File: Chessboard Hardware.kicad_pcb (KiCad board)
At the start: 2 copper layers, 199 x 199 mm, 86 parts, among them J1 Conn_01x04_Pin

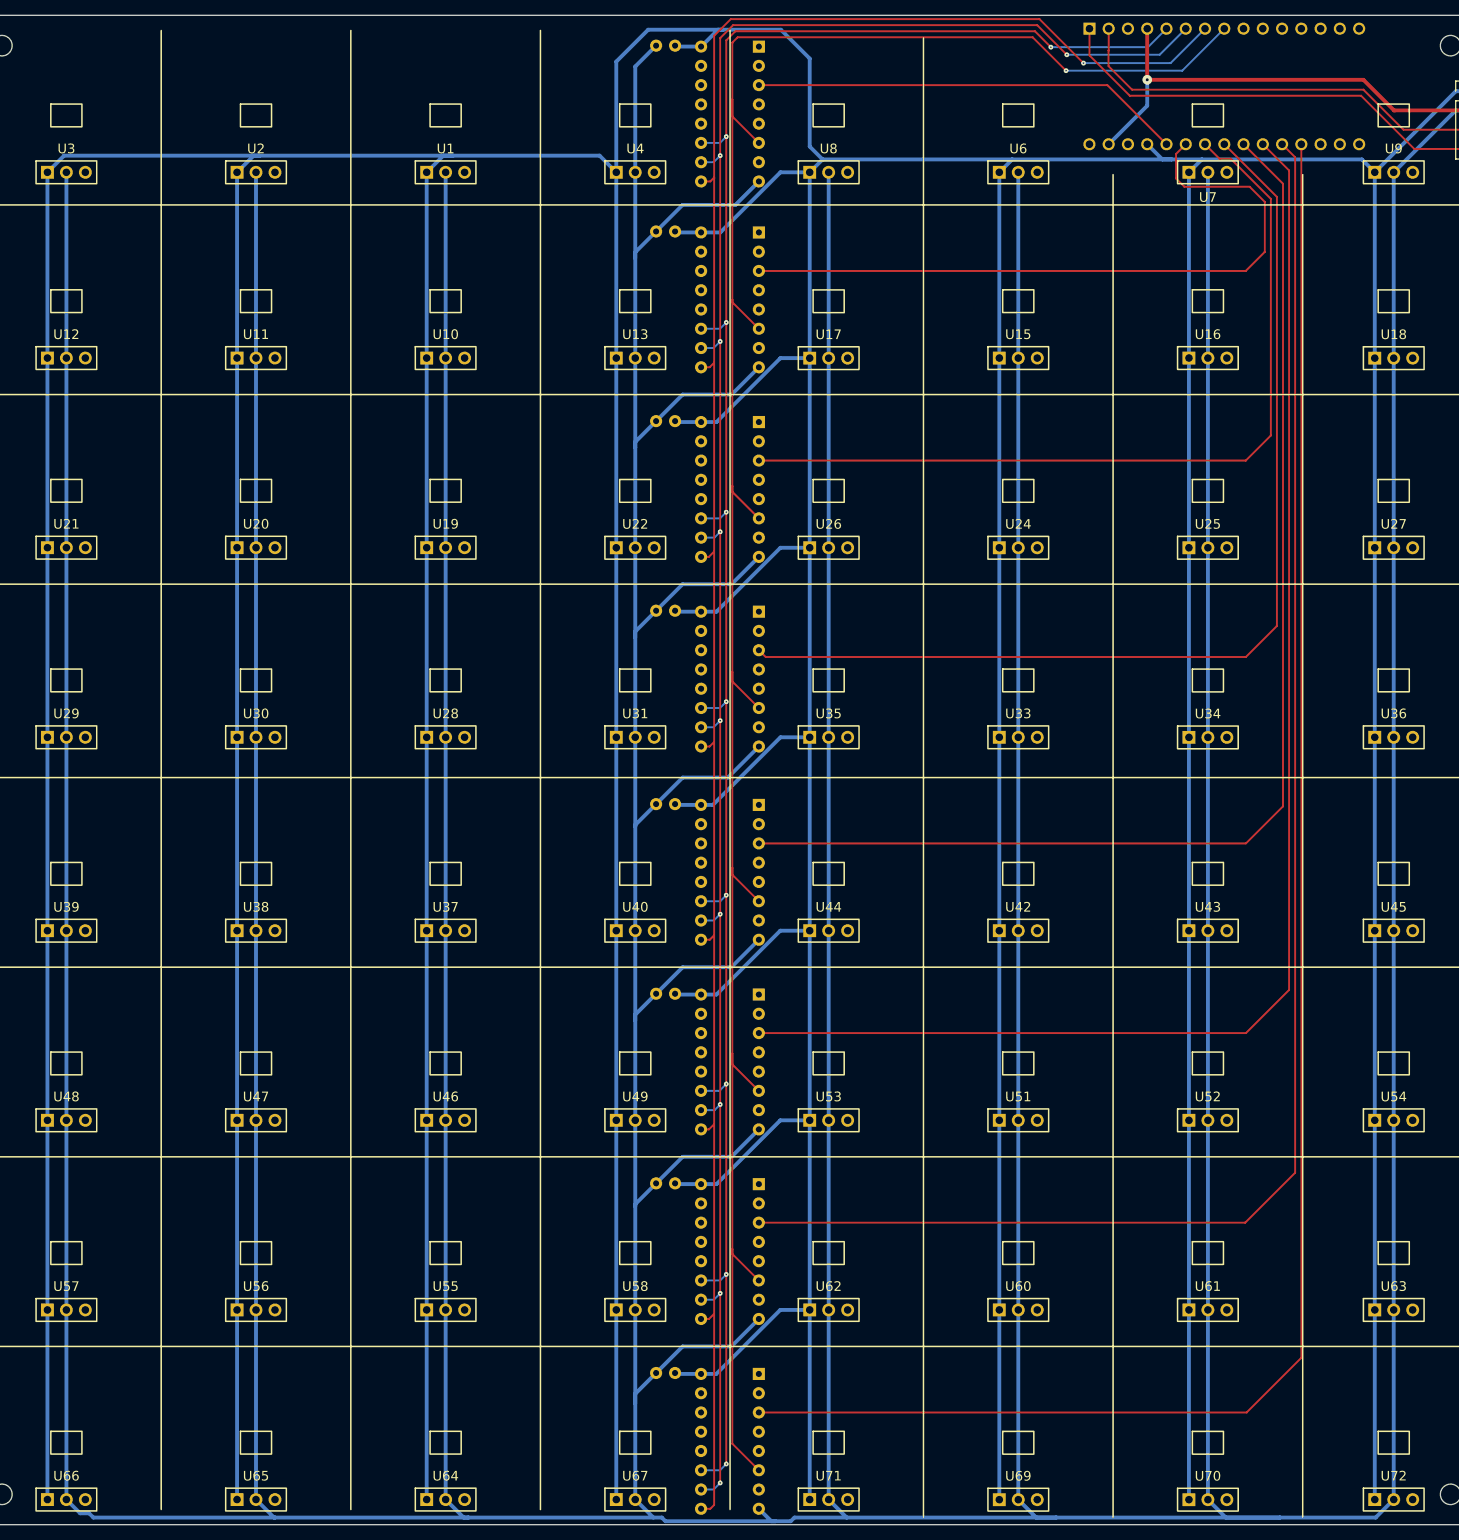
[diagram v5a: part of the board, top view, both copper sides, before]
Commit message: Finish routing
With help from Freerouting
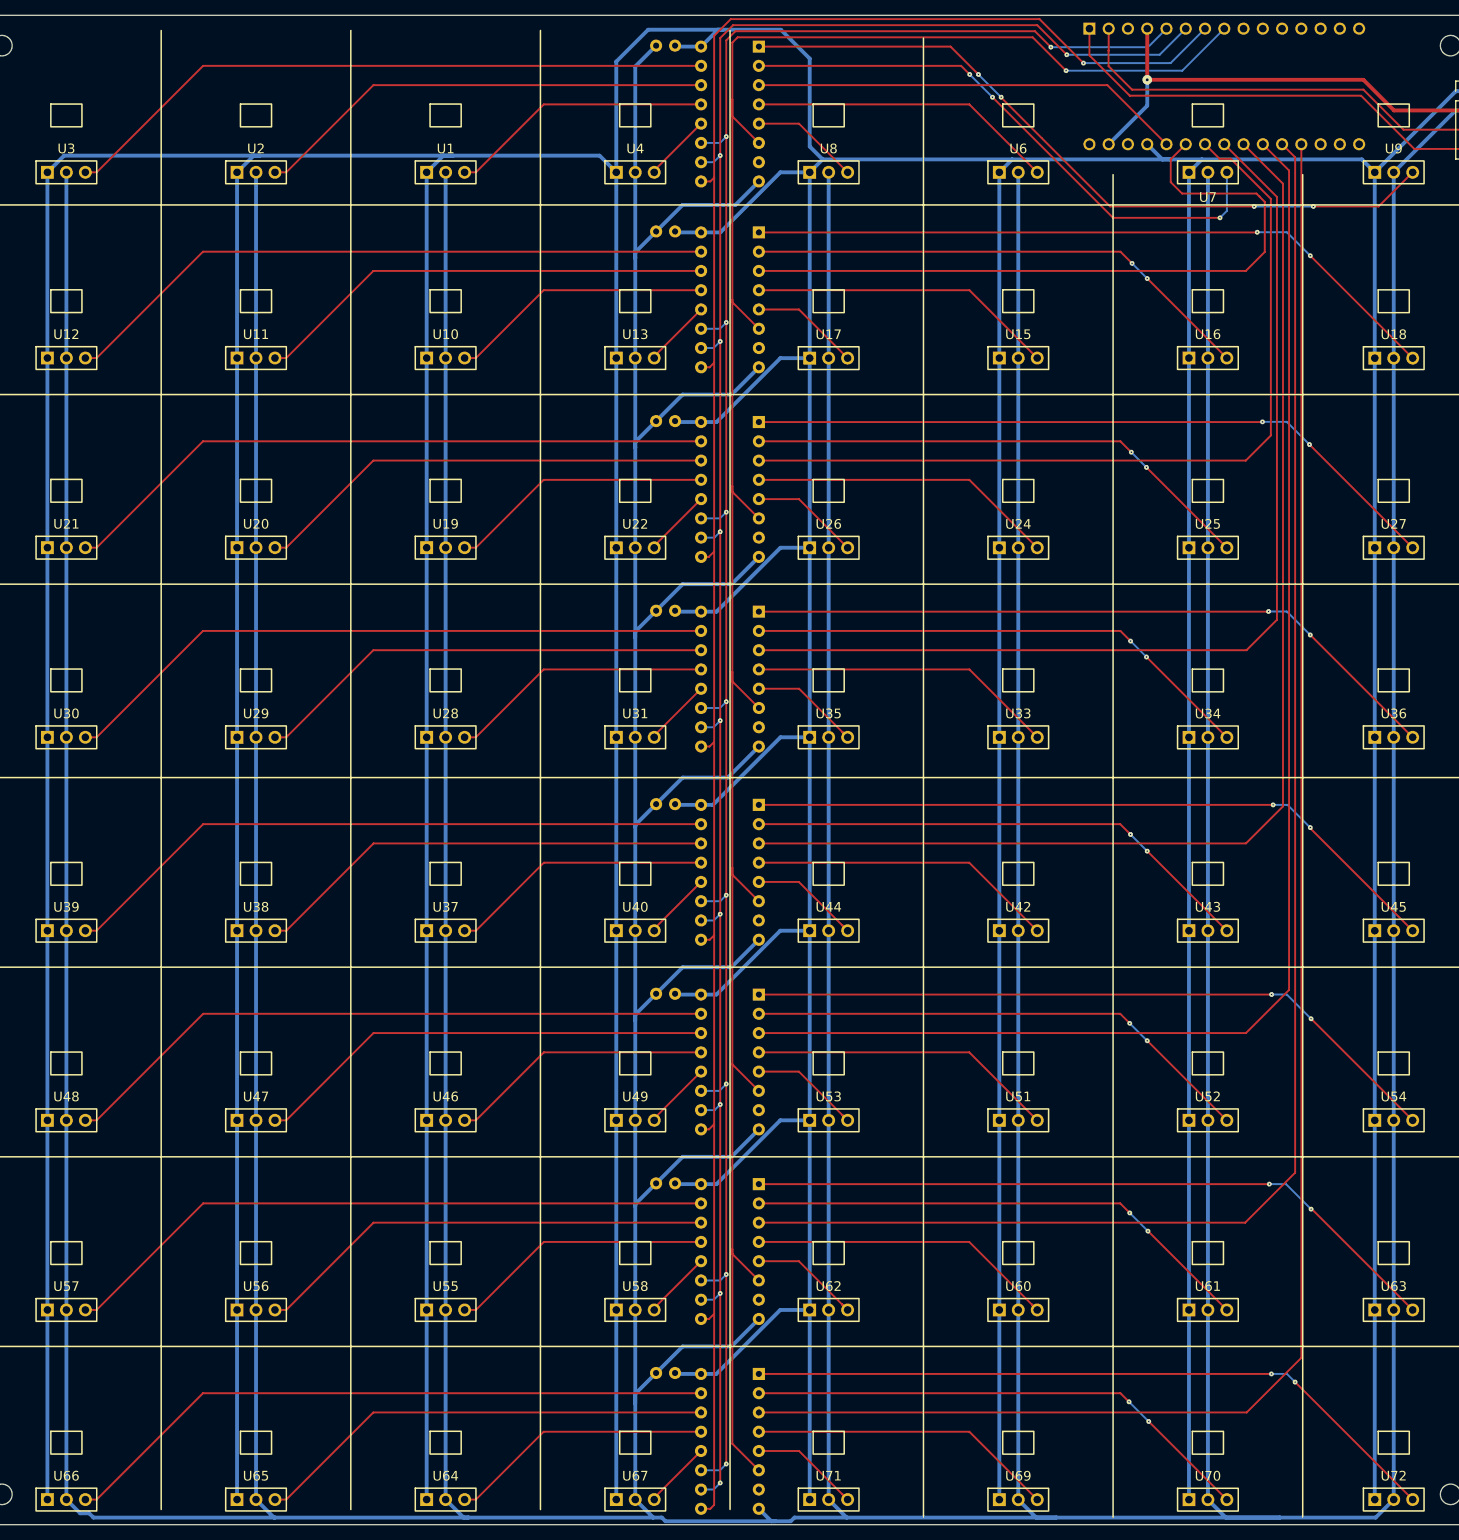
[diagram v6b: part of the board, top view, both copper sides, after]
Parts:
- moved U29 25.0 mm to (87.5, 145.2)
- moved U30 25.0 mm to (62.5, 145.2)
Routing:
- net Net-(U5-Y4): track 0.00 -> 96.8 mm, vias 0 -> 4
- net Net-(U41-Y4): track 0.00 -> 93.1 mm, vias 0 -> 2
- net Net-(U23-Y4): track 0.00 -> 93.1 mm, vias 0 -> 2
- net Net-(U14-Y4): track 0.00 -> 93.1 mm, vias 0 -> 2
- net Net-(U32-Y4): track 0.00 -> 93.1 mm, vias 0 -> 2
- net Net-(U50-Y4): track 0.00 -> 93.1 mm, vias 0 -> 2
- net Net-(U59-Y4): track 0.00 -> 93.1 mm, vias 0 -> 2
- net Net-(U68-Y4): track 0.00 -> 93.1 mm, vias 0 -> 2
- net Net-(U57-SIG): track 0.00 -> 87.0 mm
- net Net-(U39-SIG): track 0.00 -> 87.0 mm
- net Net-(U3-SIG): track 0.00 -> 87.0 mm
- net Net-(U48-SIG): track 0.00 -> 87.0 mm
- net Net-(U21-SIG): track 0.00 -> 87.0 mm
- net Net-(U30-SIG): track 0.00 -> 87.0 mm
- net Net-(U12-SIG): track 0.00 -> 87.0 mm
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
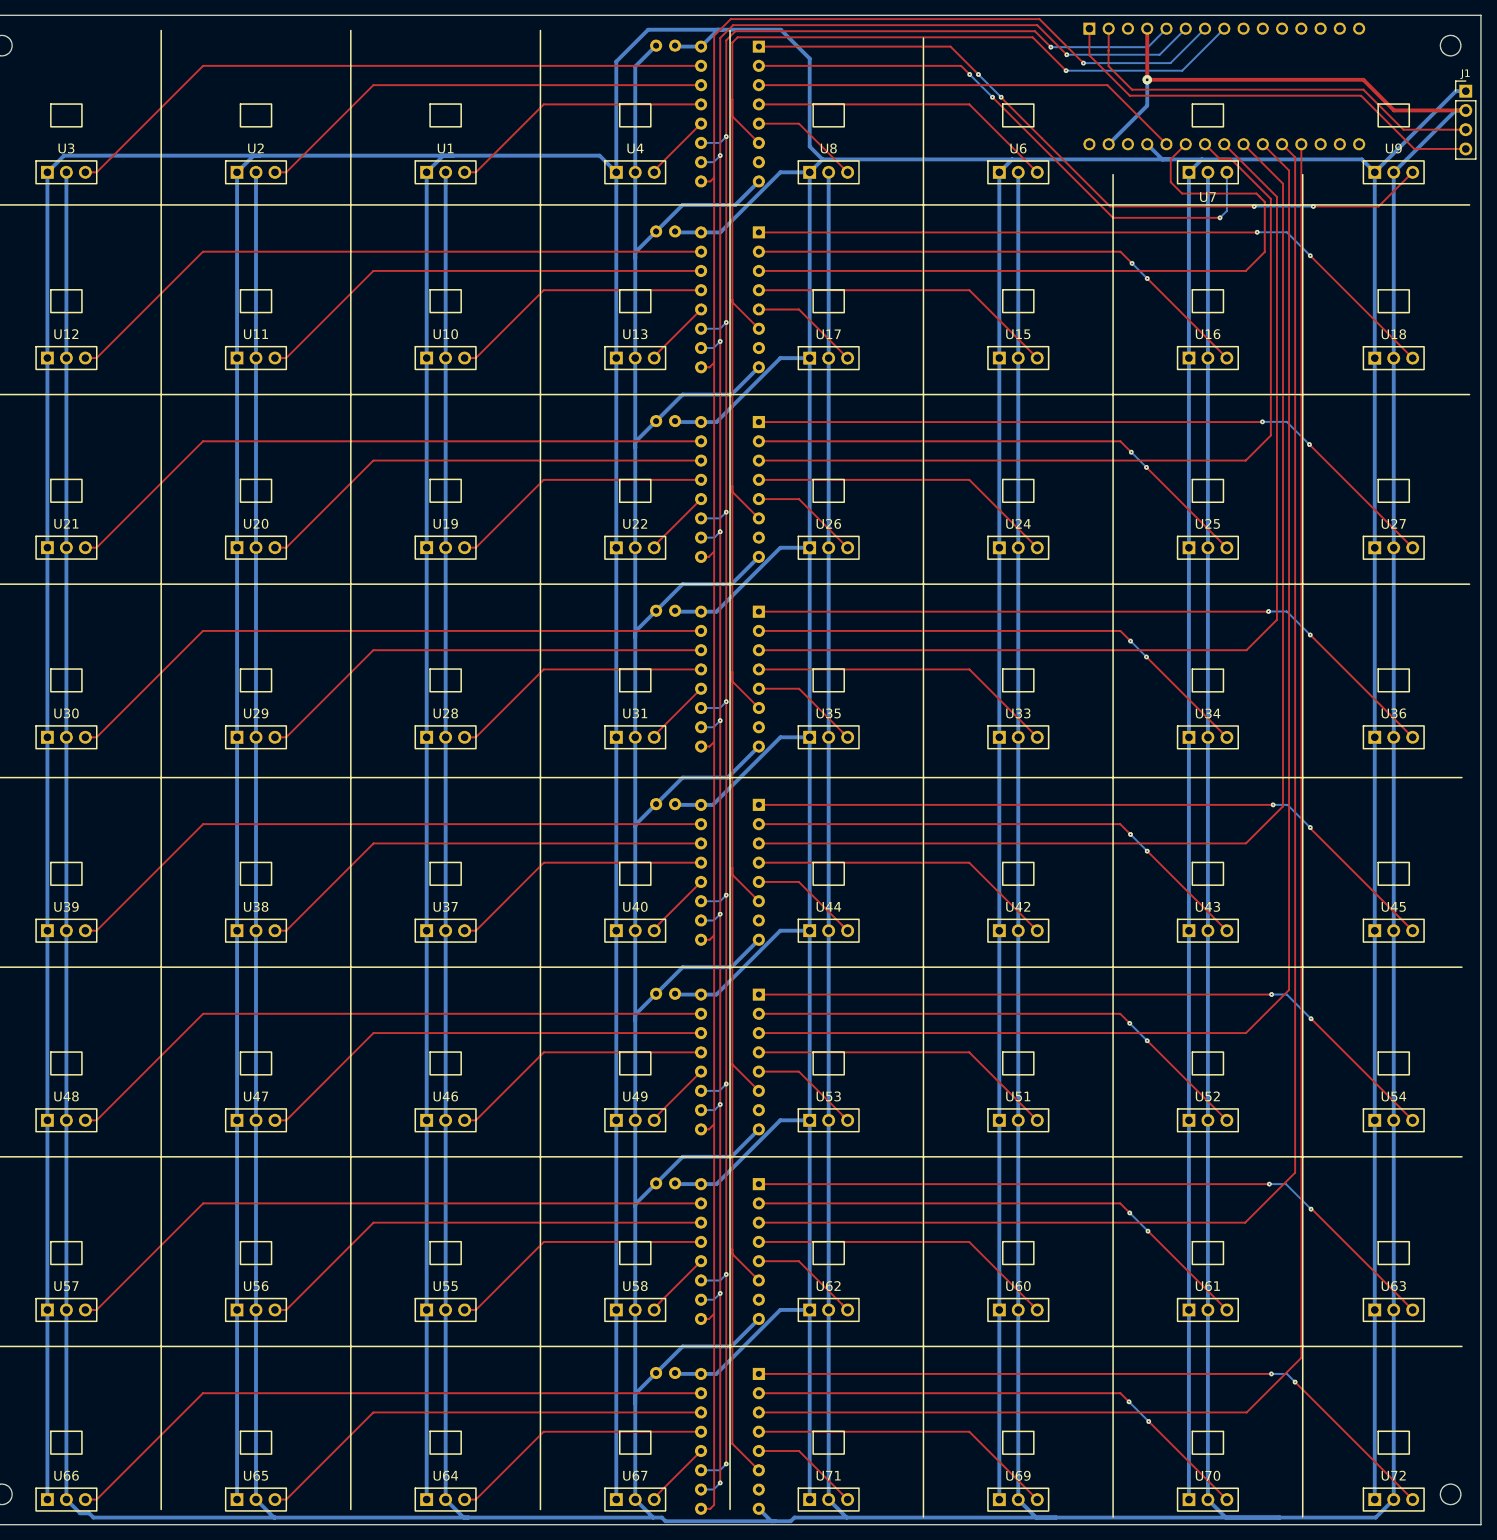
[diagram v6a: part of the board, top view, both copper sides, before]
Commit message: Cleanup routing
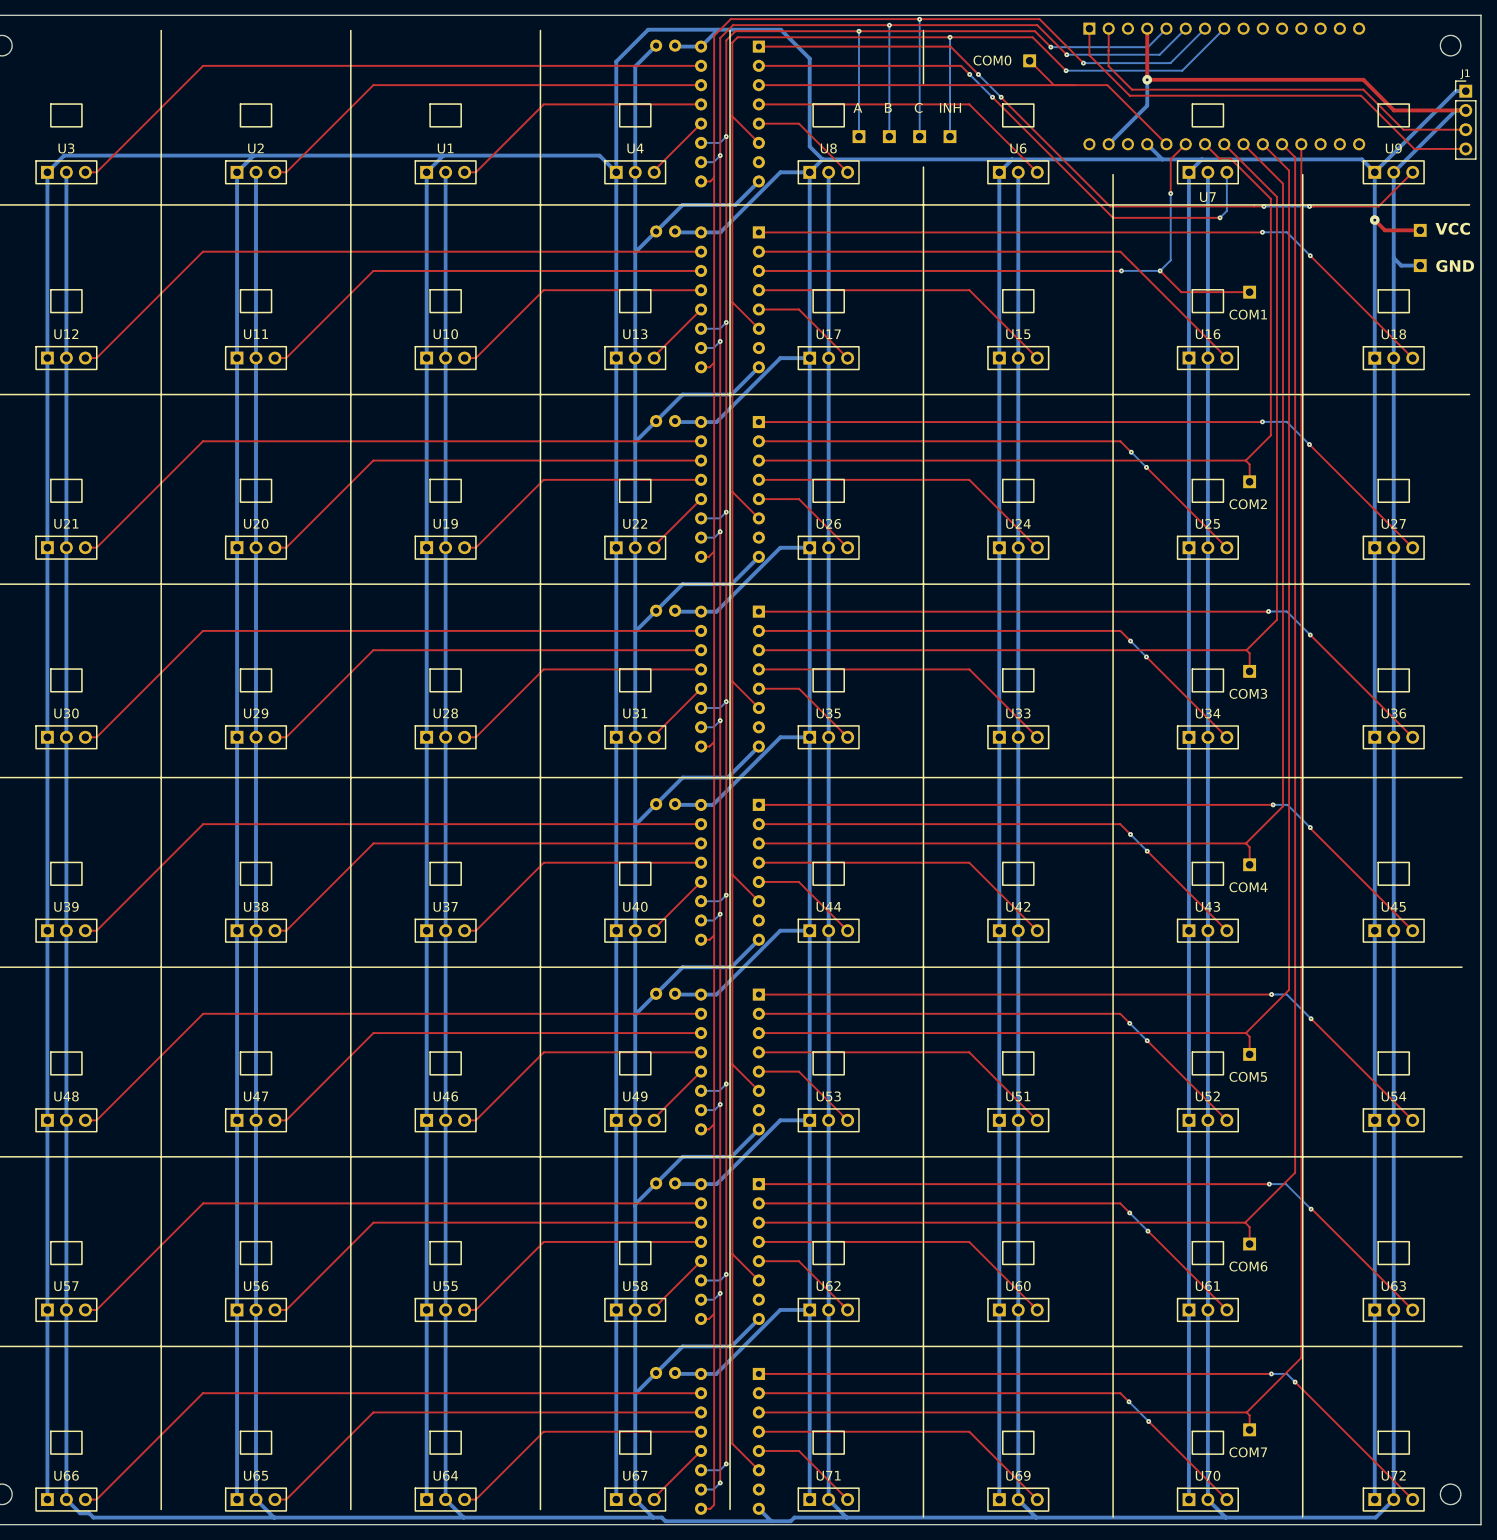
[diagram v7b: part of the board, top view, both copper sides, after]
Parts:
- added TP1: TestPoint, Connector_PinHeader_2.54mm:PinHeader_1x01_P2.54mm_Vertical, B.Cu at (241.0, 78.3)
- added TP10: TestPoint, Connector_PinHeader_2.54mm:PinHeader_1x01_P2.54mm_Vertical, B.Cu at (218.5, 136.5)
- added TP11: TestPoint, Connector_PinHeader_2.54mm:PinHeader_1x01_P2.54mm_Vertical, B.Cu at (218.5, 162.0)
- added TP12: TestPoint, Connector_PinHeader_2.54mm:PinHeader_1x01_P2.54mm_Vertical, B.Cu at (218.5, 187.0)
- added TP13: TestPoint, Connector_PinHeader_2.54mm:PinHeader_1x01_P2.54mm_Vertical, B.Cu at (218.5, 212.0)
- added TP14: TestPoint, Connector_PinHeader_2.54mm:PinHeader_1x01_P2.54mm_Vertical, B.Cu at (218.5, 236.5)
- added TP2: TestPoint, Connector_PinHeader_2.54mm:PinHeader_1x01_P2.54mm_Vertical, B.Cu at (241.0, 83.0)
- added TP3: TestPoint, Connector_PinHeader_2.54mm:PinHeader_1x01_P2.54mm_Vertical, B.Cu at (167.0, 66.0)
- added TP4: TestPoint, Connector_PinHeader_2.54mm:PinHeader_1x01_P2.54mm_Vertical, B.Cu at (171.0, 66.0)
- added TP5: TestPoint, Connector_PinHeader_2.54mm:PinHeader_1x01_P2.54mm_Vertical, B.Cu at (175.0, 66.0)
- added TP6: TestPoint, Connector_PinHeader_2.54mm:PinHeader_1x01_P2.54mm_Vertical, B.Cu at (179.0, 66.0)
- added TP7: TestPoint, Connector_PinHeader_2.54mm:PinHeader_1x01_P2.54mm_Vertical, B.Cu at (189.5, 56.0)
- added TP8: TestPoint, Connector_PinHeader_2.54mm:PinHeader_1x01_P2.54mm_Vertical, B.Cu at (218.5, 86.5)
- added TP9: TestPoint, Connector_PinHeader_2.54mm:PinHeader_1x01_P2.54mm_Vertical, B.Cu at (218.5, 111.5)
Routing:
- net /C: track 279.6 -> 294.9 mm, vias 1 -> 2
- net /B: track 278.6 -> 293.3 mm, vias 9 -> 10
- net /A: track 277.4 -> 291.3 mm, vias 9 -> 10
- net GND: track 1850.0 -> 1838.0 mm
- net /COM1: track 93.6 -> 84.0 mm, vias 0 -> 3
- net /COM0: track 57.0 -> 64.3 mm
- net /INH: track 299.6 -> 306.7 mm, vias 1 -> 2
- net /COM6: track 209.7 -> 212.8 mm
- net /COM4: track 160.6 -> 163.6 mm
- net /COM5: track 185.2 -> 188.2 mm
- net /COM2: track 111.7 -> 114.7 mm
- net /COM3: track 135.5 -> 138.5 mm
- net VCC: track 1799.9 -> 1802.6 mm, vias 0 -> 1
- net /COM7: track 234.5 -> 237.0 mm
- net Net-(U14-Y6): vias 2 -> 0
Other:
- board text added: "A"
- board text added: "B"
- board text added: "C"
- board text added: "COM0"
- board text added: "COM1"
- board text added: "COM2"
- board text added: "COM3"
- board text added: "COM4"
- board text added: "COM5"
- board text added: "COM6"
- board text added: "COM7"
- board text added: "INH"
- board text added: "VCC GND"
